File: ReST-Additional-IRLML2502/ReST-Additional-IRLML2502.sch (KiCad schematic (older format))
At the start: 16 parts, among them P1 CONN_02X07, P2 CONN_01X08, P3 SCREW_01X04, P4 SCREW_01X04, Q1 IRLML2502, Q2 IRLML2502, Q3 IRLML2502, Q4 IRLML2502

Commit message: Added BOM for all Items + suggested Links
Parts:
- P2: footprint Pin_Headers:Pin_Header_Angled_1x08 -> Pin_Headers:Pin_Header_Straight_1x08
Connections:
- net +12V: now also P1.11 (P11), P1.13 (P13), P1.5 (P5), P1.7 (P7), P1.9 (P9); no longer P1.10 (P10), P1.2 (P2), P1.4 (P4), P1.6 (P6), P1.8 (P8)
- net GND: now also P1.10 (P10), P1.12 (P12), P1.14 (P14), P1.6 (P6), P1.8 (P8); no longer P1.1 (P1), P1.3 (P3), P1.5 (P5), P1.7 (P7), P1.9 (P9)
- net PWM-ADD0: now also P1.1 (P1), R2.1; no longer P1.13 (P13), R1.1
- net PWM-ADD1: now also P1.2 (P2), R5.1; no longer P1.14 (P14), R2.1
- net PWM-ADD2: now also P1.3 (P3), R1.1; no longer P1.11 (P11), R5.1
- net PWM-ADD3: now also P1.4 (P4); no longer P1.12 (P12)
- net PWM-OUT0: now also P2.4 (P4), P4.4 (P4); no longer P2.2 (P2), P4.2 (P2)
- net PWM-OUT1: now also P2.8 (P8), P3.4 (P4); no longer P2.4 (P4), P4.4 (P4)
- net PWM-OUT3: now also P2.2 (P2), P4.2 (P2); no longer P2.8 (P8), P3.4 (P4)
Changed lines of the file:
@@
 F 3 "" H 1300 350 50  0000 C CNN
 	1    1300 1550
-	1    0    0    -1
+	-1   0    0    1
 $EndComp
 $Comp
@@
 F 0 "P2" H 1350 3300 50  0000 C CNN
 F 1 "CONN_01X08" V 1450 2850 50  0000 C CNN
-F 2 "Pin_Headers:Pin_Header_Angled_1x08" H 1350 2850 50  0001 C CNN
+F 2 "Pin_Headers:Pin_Header_Straight_1x08" H 1350 2850 50  0001 C CNN
 F 3 "" H 1350 2850 50  0000 C CNN
 	1    1350 2850
@@
 	1    0    0    -1
 $EndComp
+Text Label 1050 1750 2    39   ~ 0
+PWM-ADD3
+Text Label 1050 1850 2    39   ~ 0
+PWM-ADD1
 Text Label 1550 1750 0    39   ~ 0
-PWM-ADD3
+PWM-ADD2
 Text Label 1550 1850 0    39   ~ 0
-PWM-ADD1
-Text Label 1050 1750 2    39   ~ 0
-PWM-ADD2
-Text Label 1050 1850 2    39   ~ 0
 PWM-ADD0
 $Comp
@@
 	0    -1   -1   0
 $EndComp
-Text Label 2700 2300 2    39   ~ 0
+Text Label 2700 3750 2    39   ~ 0
 PWM-ADD0
 Text Label 3500 2000 2    39   ~ 0
@@
 	0    -1   -1   0
 $EndComp
-Text Label 2700 3750 2    39   ~ 0
+Text Label 4450 2300 2    39   ~ 0
 PWM-ADD1
 Text Label 3500 3450 2    39   ~ 0
@@
 	0    -1   -1   0
 $EndComp
-Text Label 4450 2300 2    39   ~ 0
+Text Label 2700 2300 2    39   ~ 0
 PWM-ADD2
 Text Label 5250 2000 2    39   ~ 0
@@
 	1    0    0    -1
 $EndComp
-Text Label 1050 2600 2    39   ~ 0
+Text Label 1050 2800 2    39   ~ 0
 PWM-OUT0
-Text Label 1050 2800 2    39   ~ 0
+Text Label 1050 3200 2    39   ~ 0
 PWM-OUT1
 Text Label 1050 3000 2    39   ~ 0
 PWM-OUT2
-Text Label 1050 3200 2    39   ~ 0
+Text Label 1050 2600 2    39   ~ 0
 PWM-OUT3
 $Comp

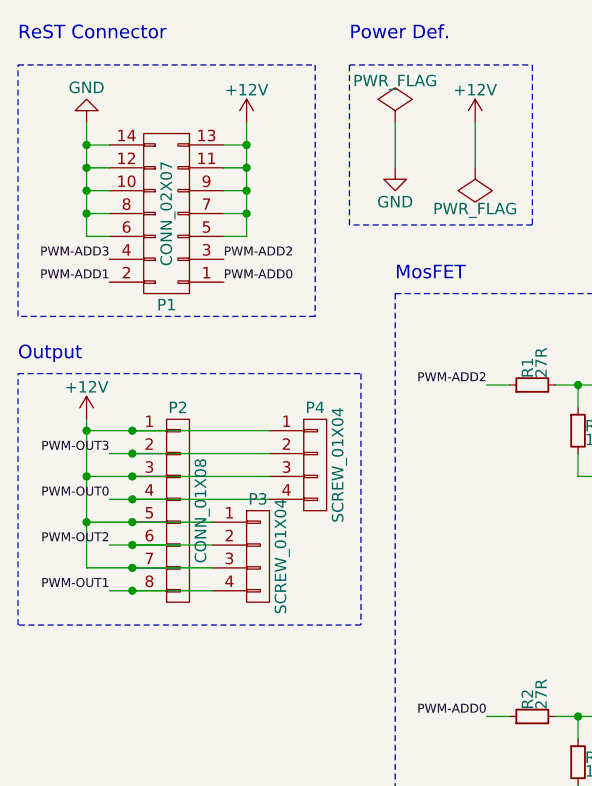
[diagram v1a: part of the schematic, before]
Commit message: Reworked Modules to sit ontop of the mainboard
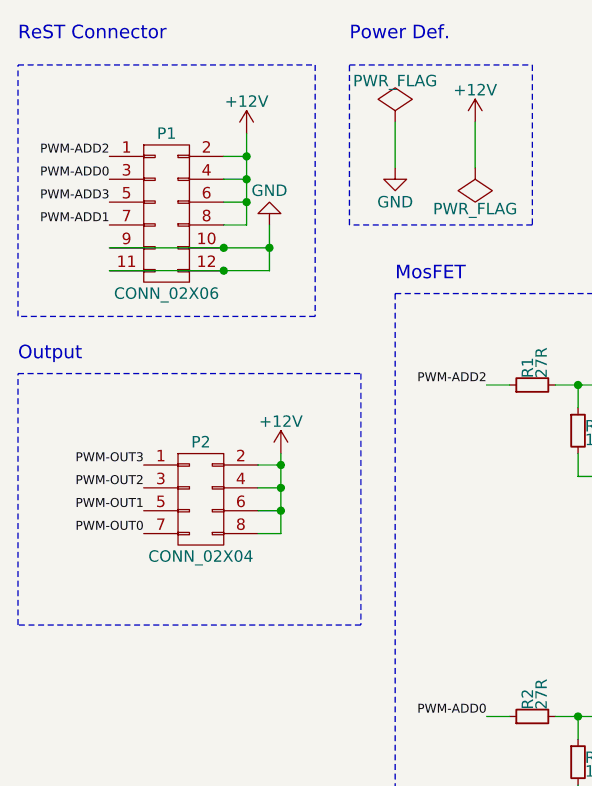
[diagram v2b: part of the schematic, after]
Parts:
- removed P1: CONN_02X07, Pin_Headers:Pin_Header_Angled_2x07, symbol CONN_02X07
- removed P2: CONN_01X08, Pin_Headers:Pin_Header_Straight_1x08, symbol CONN_01X08
- removed P3, P4: SCREW_01X04, 2:mpt_0,5%2f4-2,54, symbol CONN_01X04
- added P1: CONN_02X06, ReST-Library:bb02-hp12, symbol CONN_02X06
- added P2: CONN_02X04, Pin_Headers:Pin_Header_Straight_2x04, symbol CONN_02X04
- R1, R2, R3, R4, R5, R6, R7, R8: footprint Resistors_SMD:R_0805_HandSoldering -> Resistors_SMD:R_0603_HandSoldering
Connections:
- net +12V: now also P1.2 (P2), P1.4 (P4), P1.6 (P6), P1.8 (P8), P2.2 (P2), P2.4 (P4), P2.6 (P6), P2.8 (P8)
- net GND: now also P1.10 (P10), P1.11 (P11), P1.12 (P12), P1.9 (P9)
- net PWM-ADD0: now also P1.3 (P3)
- net PWM-ADD1: now also P1.7 (P7)
- net PWM-ADD2: now also P1.1 (P1)
- net PWM-ADD3: now also P1.5 (P5)
- net PWM-OUT0: now also P2.7 (P7)
- net PWM-OUT1: now also P2.5 (P5)
- net PWM-OUT2: now also P2.3 (P3)
- net PWM-OUT3: now also P2.1 (P1)
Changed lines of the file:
@@
 $EndDescr
-$Comp
-L CONN_02X07 P1
-U 1 1 56DAB1C3
-P 1300 1550
-F 0 "P1" H 1300 1950 50  0000 C CNN
-F 1 "CONN_02X07" V 1300 1550 50  0000 C CNN
-F 2 "Pin_Headers:Pin_Header_Angled_2x07" H 1300 350 50  0001 C CNN
-F 3 "" H 1300 350 50  0000 C CNN
-	1    1300 1550
-	-1   0    0    1
-$EndComp
-$Comp
-L CONN_01X08 P2
-U 1 1 56DAB1DA
-P 1350 2850
-F 0 "P2" H 1350 3300 50  0000 C CNN
-F 1 "CONN_01X08" V 1450 2850 50  0000 C CNN
-F 2 "Pin_Headers:Pin_Header_Straight_1x08" H 1350 2850 50  0001 C CNN
-F 3 "" H 1350 2850 50  0000 C CNN
-	1    1350 2850
-	1    0    0    -1
-$EndComp
 $Comp
 L Q_NMOS_GSD Q1
@@
 L +12V #PWR01
 U 1 1 56DAB626
-P 1650 1150
-F 0 "#PWR01" H 1650 1000 50  0001 C CNN
-F 1 "+12V" H 1650 1290 50  0000 C CNN
-F 2 "" H 1650 1150 50  0000 C CNN
-F 3 "" H 1650 1150 50  0000 C CNN
-	1    1650 1150
+P 1650 1200
+F 0 "#PWR01" H 1650 1050 50  0001 C CNN
+F 1 "+12V" H 1650 1340 50  0000 C CNN
+F 2 "" H 1650 1200 50  0000 C CNN
+F 3 "" H 1650 1200 50  0000 C CNN
+	1    1650 1200
 	1    0    0    -1
 $EndComp
@@
 L GND #PWR02
 U 1 1 56DAB648
-P 950 1150
-F 0 "#PWR02" H 950 900 50  0001 C CNN
-F 1 "GND" H 950 1000 50  0000 C CNN
-F 2 "" H 950 1150 50  0000 C CNN
-F 3 "" H 950 1150 50  0000 C CNN
-	1    950  1150
+P 1750 1600
+F 0 "#PWR02" H 1750 1350 50  0001 C CNN
+F 1 "GND" H 1750 1450 50  0000 C CNN
+F 2 "" H 1750 1600 50  0000 C CNN
+F 3 "" H 1750 1600 50  0000 C CNN
+	1    1750 1600
 	-1   0    0    1
 $EndComp
@@
 F 0 "R3" H 3130 2520 50  0000 L CNN
 F 1 "100K" H 3130 2460 50  0000 L CNN
-F 2 "Resistors_SMD:R_0805_HandSoldering" H 3100 2500 50  0001 C CNN
+F 2 "Resistors_SMD:R_0603_HandSoldering" H 3100 2500 50  0001 C CNN
 F 3 "" H 3100 2500 50  0000 C CNN
 	1    3100 2500
 	1    0    0    -1
 $EndComp
-Text Label 1050 1750 2    39   ~ 0
+Text Label 1050 1500 2    39   ~ 0
 PWM-ADD3
-Text Label 1050 1850 2    39   ~ 0
+Text Label 1050 1600 2    39   ~ 0
 PWM-ADD1
-Text Label 1550 1750 0    39   ~ 0
+Text Label 1050 1300 2    39   ~ 0
 PWM-ADD2
-Text Label 1550 1850 0    39   ~ 0
+Text Label 1050 1400 2    39   ~ 0
 PWM-ADD0
 $Comp
@@
 F 0 "R1" H 2930 2320 50  0000 L CNN
 F 1 "27R" H 2930 2260 50  0000 L CNN
-F 2 "Resistors_SMD:R_0805_HandSoldering" H 2900 2300 50  0001 C CNN
+F 2 "Resistors_SMD:R_0603_HandSoldering" H 2900 2300 50  0001 C CNN
 F 3 "" H 2900 2300 50  0000 C CNN
 	1    2900 2300
@@
 F 0 "R4" H 3130 3970 50  0000 L CNN
 F 1 "100K" H 3130 3910 50  0000 L CNN
-F 2 "Resistors_SMD:R_0805_HandSoldering" H 3100 3950 50  0001 C CNN
+F 2 "Resistors_SMD:R_0603_HandSoldering" H 3100 3950 50  0001 C CNN
 F 3 "" H 3100 3950 50  0000 C CNN
 	1    3100 3950
@@
 F 0 "R2" H 2930 3770 50  0000 L CNN
 F 1 "27R" H 2930 3710 50  0000 L CNN
-F 2 "Resistors_SMD:R_0805_HandSoldering" H 2900 3750 50  0001 C CNN
+F 2 "Resistors_SMD:R_0603_HandSoldering" H 2900 3750 50  0001 C CNN
 F 3 "" H 2900 3750 50  0000 C CNN
 	1    2900 3750
@@
 F 0 "R7" H 4880 2520 50  0000 L CNN
 F 1 "100K" H 4880 2460 50  0000 L CNN
-F 2 "Resistors_SMD:R_0805_HandSoldering" H 4850 2500 50  0001 C CNN
+F 2 "Resistors_SMD:R_0603_HandSoldering" H 4850 2500 50  0001 C CNN
 F 3 "" H 4850 2500 50  0000 C CNN
 	1    4850 2500
@@
 F 0 "R5" H 4680 2320 50  0000 L CNN
 F 1 "27R" H 4680 2260 50  0000 L CNN
-F 2 "Resistors_SMD:R_0805_HandSoldering" H 4650 2300 50  0001 C CNN
+F 2 "Resistors_SMD:R_0603_HandSoldering" H 4650 2300 50  0001 C CNN
 F 3 "" H 4650 2300 50  0000 C CNN
 	1    4650 2300
@@
 F 0 "R8" H 4880 3970 50  0000 L CNN
 F 1 "100K" H 4880 3910 50  0000 L CNN
-F 2 "Resistors_SMD:R_0805_HandSoldering" H 4850 3950 50  0001 C CNN
+F 2 "Resistors_SMD:R_0603_HandSoldering" H 4850 3950 50  0001 C CNN
 F 3 "" H 4850 3950 50  0000 C CNN
 	1    4850 3950
@@
 F 0 "R6" H 4680 3770 50  0000 L CNN
 F 1 "27R" H 4680 3710 50  0000 L CNN
-F 2 "Resistors_SMD:R_0805_HandSoldering" H 4650 3750 50  0001 C CNN
+F 2 "Resistors_SMD:R_0603_HandSoldering" H 4650 3750 50  0001 C CNN
 F 3 "" H 4650 3750 50  0000 C CNN
 	1    4650 3750
@@
 	1    0    0    -1
 $EndComp
-Text Label 1050 2800 2    39   ~ 0
+Text Label 1200 2950 2    39   ~ 0
 PWM-OUT0
-Text Label 1050 3200 2    39   ~ 0
+Text Label 1200 2850 2    39   ~ 0
 PWM-OUT1
-Text Label 1050 3000 2    39   ~ 0
+Text Label 1200 2750 2    39   ~ 0
 PWM-OUT2
-Text Label 1050 2600 2    39   ~ 0
+Text Label 1200 2650 2    39   ~ 0
 PWM-OUT3
 $Comp
 L +12V #PWR011
 U 1 1 56DAE15F
-P 950 2450
-F 0 "#PWR011" H 950 2300 50  0001 C CNN
-F 1 "+12V" H 950 2590 50  0000 C CNN
-F 2 "" H 950 2450 50  0000 C CNN
-F 3 "" H 950 2450 50  0000 C CNN
-	1    950  2450
-	1    0    0    -1
-$EndComp
-Wire Wire Line
-	1650 1650 1550 1650
-Wire Wire Line
-	1650 1150 1650 1650
-Wire Wire Line
-	1550 1550 1650 1550
-Connection ~ 1650 1550
-Wire Wire Line
-	1550 1450 1650 1450
-Connection ~ 1650 1450
-Wire Wire Line
-	1550 1350 1650 1350
-Connection ~ 1650 1350
-Wire Wire Line
-	1550 1250 1650 1250
-Connection ~ 1650 1250
-Wire Wire Line
-	950  1150 950  1650
-Wire Wire Line
-	950  1650 1050 1650
-Wire Wire Line
-	1050 1550 950  1550
-Connection ~ 950  1550
-Wire Wire Line
-	1050 1450 950  1450
-Connection ~ 950  1450
-Wire Wire Line
-	1050 1350 950  1350
-Connection ~ 950  1350
-Wire Wire Line
-	1050 1250 950  1250
-Connection ~ 950  1250
+P 1800 2600
+F 0 "#PWR011" H 1800 2450 50  0001 C CNN
+F 1 "+12V" H 1800 2740 50  0000 C CNN
+F 2 "" H 1800 2600 50  0000 C CNN
+F 3 "" H 1800 2600 50  0000 C CNN
+	1    1800 2600
+	1    0    0    -1
+$EndComp
+Wire Wire Line
+	1650 1600 1550 1600
+Wire Wire Line
+	1650 1200 1650 1600
+Wire Wire Line
+	1550 1500 1650 1500
+Connection ~ 1650 1500
+Wire Wire Line
+	1550 1400 1650 1400
+Connection ~ 1650 1400
+Wire Wire Line
+	1550 1300 1650 1300
+Connection ~ 1650 1300
 Wire Wire Line
 	2300 1350 2300 1150
@@
 	5250 3950 5250 4250
 Connection ~ 5250 4150
-Wire Wire Line
-	1050 2600 1750 2600
-Connection ~ 1150 2600
-Wire Wire Line
-	1050 3000 1500 3000
-Wire Wire Line
-	1050 3200 1500 3200
-Wire Wire Line
-	1050 2800 1750 2800
-Connection ~ 1150 2800
-Connection ~ 1150 3000
-Connection ~ 1150 3200
-Wire Wire Line
-	950  2450 950  3100
-Wire Wire Line
-	950  3100 1500 3100
-Wire Wire Line
-	950  2900 1500 2900
-Connection ~ 950  2900
-Wire Wire Line
-	950  2700 1750 2700
-Connection ~ 950  2700
-Wire Wire Line
-	950  2500 1750 2500
-Connection ~ 950  2500
-Connection ~ 1150 2500
-Connection ~ 1150 2700
-Connection ~ 1150 2900
-Connection ~ 1150 3100
-$Comp
-L CONN_01X04 P4
-U 1 1 56DAF75A
-P 1950 2650
-F 0 "P4" H 1950 2900 50  0000 C CNN
-F 1 "SCREW_01X04" V 2050 2650 50  0000 C CNN
-F 2 "2:mpt_0,5%2f4-2,54" H 1950 2650 50  0001 C CNN
-F 3 "" H 1950 2650 50  0000 C CNN
-	1    1950 2650
-	1    0    0    -1
-$EndComp
-$Comp
-L CONN_01X04 P3
-U 1 1 56DAF7C3
-P 1700 3050
-F 0 "P3" H 1700 3300 50  0000 C CNN
-F 1 "SCREW_01X04" V 1800 3050 50  0000 C CNN
-F 2 "2:mpt_0,5%2f4-2,54" H 1700 3050 50  0001 C CNN
-F 3 "" H 1700 3050 50  0000 C CNN
-	1    1700 3050
-	1    0    0    -1
-$EndComp
 Wire Notes Line
 	650  2250 2150 2250
@@
 Text Notes 2300 1850 0    59   ~ 0
 MosFET
+$Comp
+L CONN_02X06 P1
+U 1 1 57367526
+P 1300 1550
+F 0 "P1" H 1300 1900 50  0000 C CNN
+F 1 "CONN_02X06" H 1300 1200 50  0000 C CNN
+F 2 "ReST-Library:bb02-hp12" H 1300 350 50  0001 C CNN
+F 3 "" H 1300 350 50  0000 C CNN
+	1    1300 1550
+	1    0    0    -1
+$EndComp
+$Comp
+L CONN_02X04 P2
+U 1 1 57367C7C
+P 1450 2800
+F 0 "P2" H 1450 3050 50  0000 C CNN
+F 1 "CONN_02X04" H 1450 2550 50  0000 C CNN
+F 2 "Pin_Headers:Pin_Header_Straight_2x04" H 1450 1600 50  0001 C CNN
+F 3 "" H 1450 1600 50  0000 C CNN
+	1    1450 2800
+	1    0    0    -1
+$EndComp
+Wire Wire Line
+	1800 2600 1800 2950
+Wire Wire Line
+	1800 2650 1700 2650
+Wire Wire Line
+	1800 2750 1700 2750
+Connection ~ 1800 2650
+Wire Wire Line
+	1800 2850 1700 2850
+Connection ~ 1800 2750
+Wire Wire Line
+	1800 2950 1700 2950
+Connection ~ 1800 2850
+Wire Wire Line
+	1750 1800 1750 1600
+Wire Wire Line
+	1050 1700 1750 1700
+Connection ~ 1550 1700
+Wire Wire Line
+	1050 1800 1750 1800
+Connection ~ 1750 1700
+Connection ~ 1550 1800
 $EndSCHEMATC
